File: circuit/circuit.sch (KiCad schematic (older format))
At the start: 4 parts, among them SW1 SW_Push, U1 ESP32_DevKit

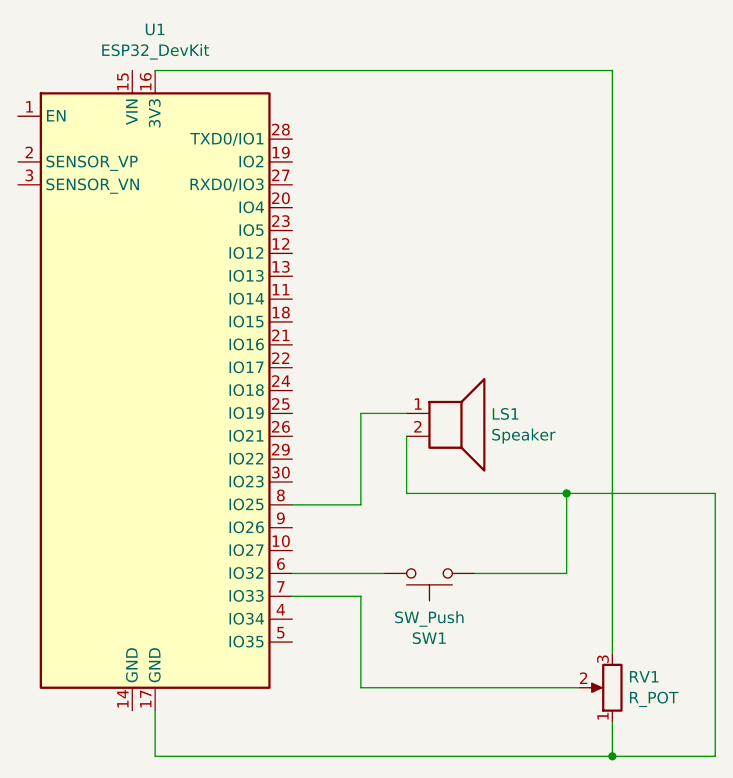
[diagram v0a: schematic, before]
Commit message: add a capacitor to audio signal to add DC offset
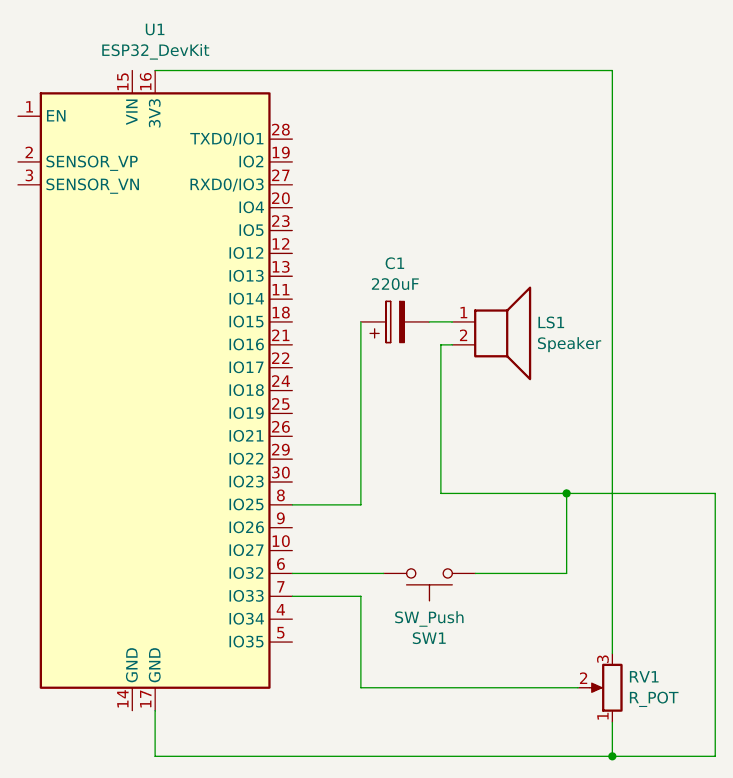
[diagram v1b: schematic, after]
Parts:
- added C1: 220uF, symbol Device:CP
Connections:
- net at LS1.1: now also C1.2; no longer U1.8 (IO25)
- new net: C1.1, U1.8 (IO25)
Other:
- moved on the sheet: LS1
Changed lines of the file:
@@
 L Device:Speaker LS1
 U 1 1 600EEE8B
-P 6500 3800
-F 0 "LS1" H 6670 3796 50  0000 L CNN
-F 1 "Speaker" H 6670 3705 50  0000 L CNN
-F 2 "" H 6500 3600 50  0001 C CNN
-F 3 "~" H 6490 3750 50  0001 C CNN
-	1    6500 3800
+P 6700 3400
+F 0 "LS1" H 6870 3396 50  0000 L CNN
+F 1 "Speaker" H 6870 3305 50  0000 L CNN
+F 2 "" H 6700 3200 50  0001 C CNN
+F 3 "~" H 6690 3350 50  0001 C CNN
+	1    6700 3400
 	1    0    0    -1
 $EndComp
@@
 	5800 4200 6100 4200
 Wire Wire Line
-	6100 4200 6100 3800
-Wire Wire Line
-	6100 3800 6300 3800
-Wire Wire Line
 	6100 4600 6100 5000
 Wire Wire Line
@@
 	7650 4150 7000 4150
 Wire Wire Line
-	6300 4150 6300 3900
-Wire Wire Line
 	7200 5150 7200 5300
 Wire Wire Line
@@
 Wire Wire Line
 	7000 4500 7000 4150
-Connection ~ 7000 4150
-Wire Wire Line
-	7000 4150 6300 4150
 Wire Wire Line
 	5200 2300 7200 2300
@@
 Wire Wire Line
 	5200 5300 7200 5300
+$Comp
+L Device:CP C1
+U 1 1 602014E6
+P 6250 3400
+F 0 "C1" V 6505 3400 50  0000 C CNN
+F 1 "220uF" V 6414 3400 50  0000 C CNN
+F 2 "" H 6288 3250 50  0001 C CNN
+F 3 "~" H 6250 3400 50  0001 C CNN
+	1    6250 3400
+	0    -1   -1   0
+$EndComp
+Wire Wire Line
+	6400 3400 6500 3400
+Wire Wire Line
+	6100 3400 6100 4200
+Wire Wire Line
+	6500 3500 6450 3500
+Wire Wire Line
+	6450 3500 6450 4150
+Wire Wire Line
+	6450 4150 7000 4150
+Connection ~ 7000 4150
 $EndSCHEMATC
